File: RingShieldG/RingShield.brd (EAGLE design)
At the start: 70 x 140 mm, 28 parts

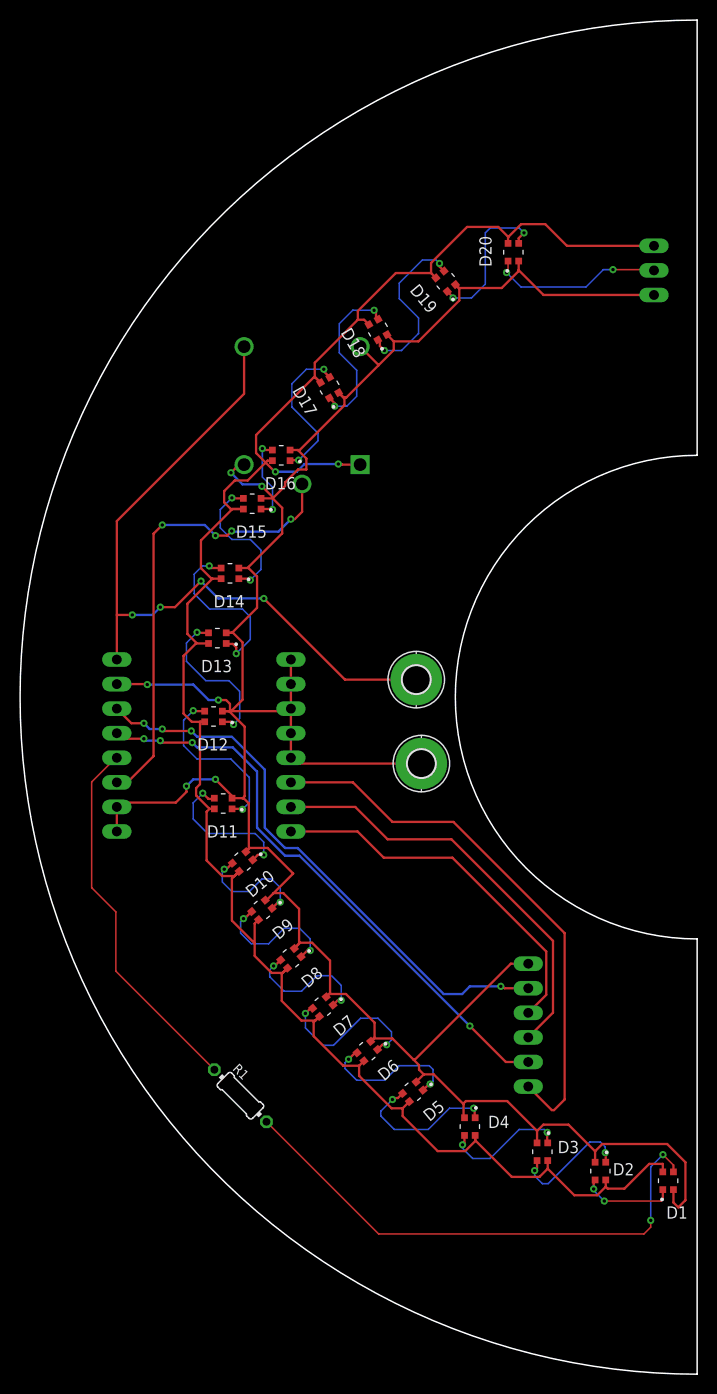
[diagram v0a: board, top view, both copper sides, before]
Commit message: Updating leds to correct orientation
Leads to less via's used
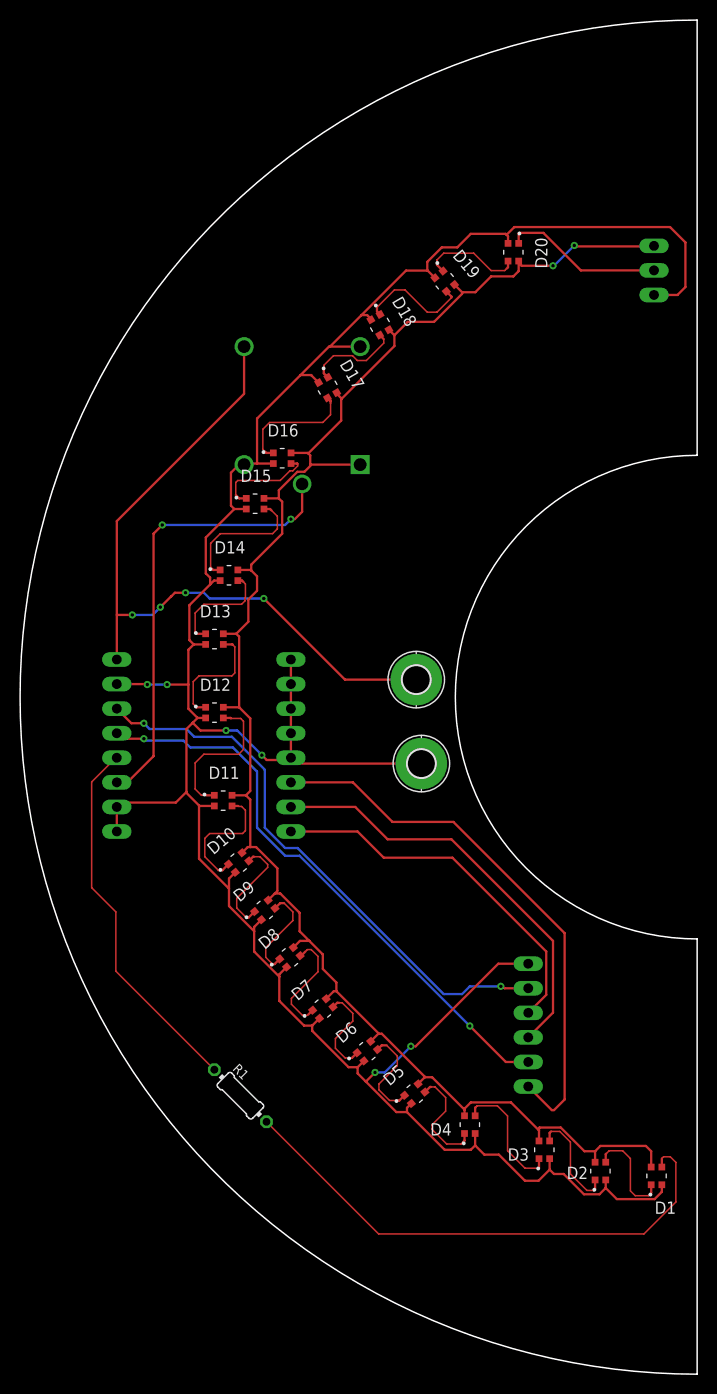
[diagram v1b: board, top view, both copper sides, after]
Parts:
- moved D1 1.30 mm to (65.8, 20.5)
- moved D18 0.54 mm to (37.2, 108.5), turned to 300 degrees
- moved D12 0.41 mm to (20.1, 68.4), turned to 0 degrees
- moved D10 0.41 mm to (22.6, 52.9), turned to 40 degrees
- moved D16 0.32 mm to (27.1, 94.7), turned to 0 degrees
- moved D13 0.32 mm to (20.1, 76.0), turned to 0 degrees
- moved D15 0.30 mm to (24.3, 90.0), turned to 0 degrees
- moved D9 0.30 mm to (25.3, 48.0), turned to 40 degrees
- moved D11 0.30 mm to (21.0, 59.3), turned to 0 degrees
- moved D3 0.28 mm to (54.2, 23.2), turned to 90 degrees
- moved D5 0.28 mm to (40.8, 29.0), turned to 40 degrees
- moved D14 0.22 mm to (21.6, 82.6), turned to 0 degrees
- moved D7 0.20 mm to (31.3, 37.8), turned to 40 degrees
- moved D17 0.20 mm to (31.8, 102.0), turned to 300 degrees
- moved D4 0.20 mm to (46.5, 25.8), turned to 90 degrees
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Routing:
- net +5V: track 213.2 -> 183.4 mm
- net N$19: track 17.3 -> 9.98 mm, vias 2 -> 0
- net N$14: track 18.3 -> 11.5 mm, vias 2 -> 0
- net N$12: track 16.5 -> 9.91 mm, vias 2 -> 0
- net N$7: track 18.0 -> 11.8 mm, vias 2 -> 0
- net GND: track 281.1 -> 286.5 mm
- net N$22: track 15.9 -> 10.6 mm, vias 2 -> 0
- net N$6: track 15.4 -> 10.3 mm, vias 2 -> 0
- net N$5: track 15.6 -> 11.6 mm, vias 2 -> 0
- net N$15: track 16.4 -> 12.4 mm, vias 2 -> 0
- net N$10: track 14.0 -> 10.3 mm, vias 2 -> 0
- net N$20: track 15.8 -> 12.8 mm, vias 2 -> 0
- net N$11: track 14.0 -> 11.4 mm, vias 2 -> 0
- net N$16: track 18.1 -> 15.7 mm, vias 2 -> 0
- net N$17: track 15.5 -> 13.4 mm, vias 2 -> 0
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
